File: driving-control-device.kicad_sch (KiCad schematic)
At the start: 5 parts, among them J1 Micro_SD_Card, U1 MPU-6050, U2 NEO-M9N, U3 SIM900

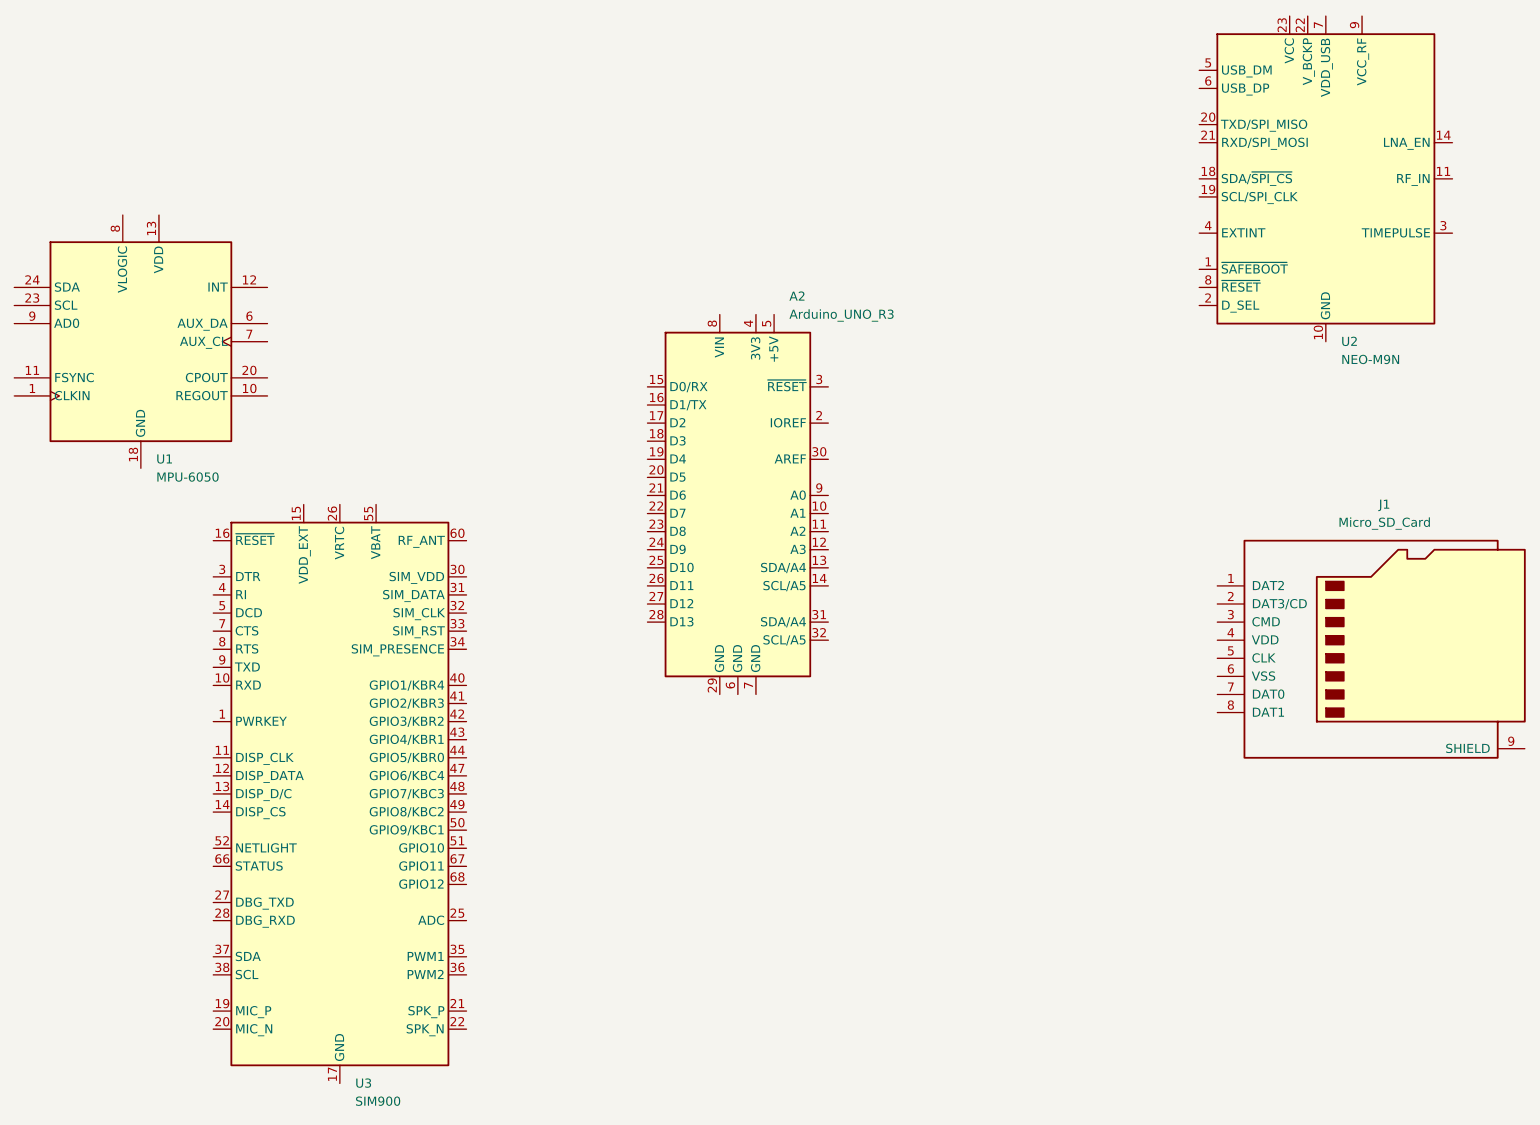
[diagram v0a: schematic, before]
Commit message: upd: principial schematic
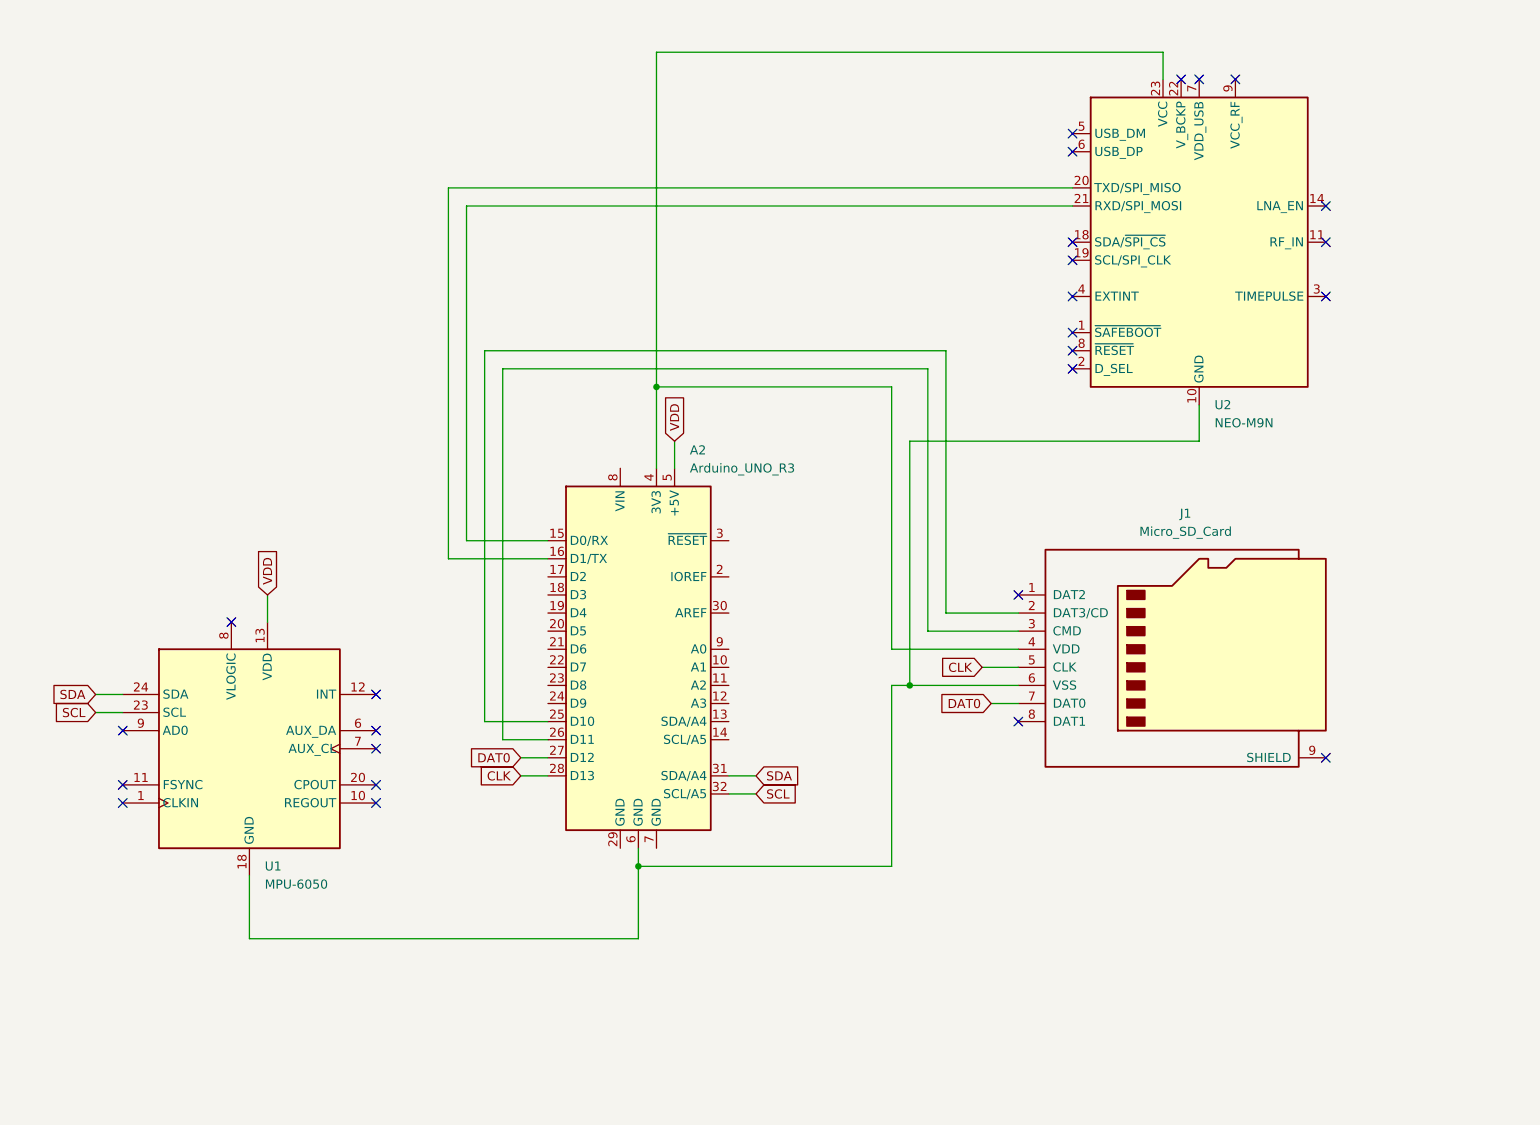
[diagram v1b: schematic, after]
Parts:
- removed U3: SIM900, RF_GSM:SIMCom_SIM900, symbol RF_GSM:SIM900
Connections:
- net at J1.2 (DAT3/CD): now also A2.25 (D10)
- net at J1.3 (CMD): now also A2.26 (D11)
- net at J1.4 (VDD): now also A2.4 (3V3), U2.23 (VCC)
- net CLK: now reaches J1.5 (CLK)
- net CLK: now also A2.28 (D13)
- net at J1.6 (VSS): now also A2.6 (GND), U1.18 (GND), U2.10 (GND), U2.12 (GND), U2.13 (GND), U2.24 (GND)
- net DAT0: now reaches J1.7 (DAT0)
- net DAT0: now also A2.27 (D12)
- net VDD: now reaches U1.13 (VDD)
- net VDD: now also A2.5 (+5V)
- net SCL: now reaches U1.23 (SCL)
- net SCL: now also A2.32 (SCL/A5)
- net SDA: now reaches U1.24 (SDA)
- net SDA: now also A2.31 (SDA/A4)
- net at A2.15 (D0/RX): now also U2.21 (RXD/SPI_MOSI)
- net at A2.16 (D1/TX): now also U2.20 (TXD/SPI_MISO)
- no-connect marks 0 -> 26
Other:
- moved on the sheet: A2, J1, U1, U2
